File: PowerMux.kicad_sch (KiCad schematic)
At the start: 44 parts, among them J1 USB_C_Receptacle_USB2.0, J3 Barrel_Jack_Switch, J5 USB_B_Mini, J6 Conn_01x04_Socket, Q3 DMP3036SSD, SW1 SW_SPST, U11 L78L05_SOT89, U2 USBLC6-2SC6, U4 CH32X035G8U6, U8 AO3400A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

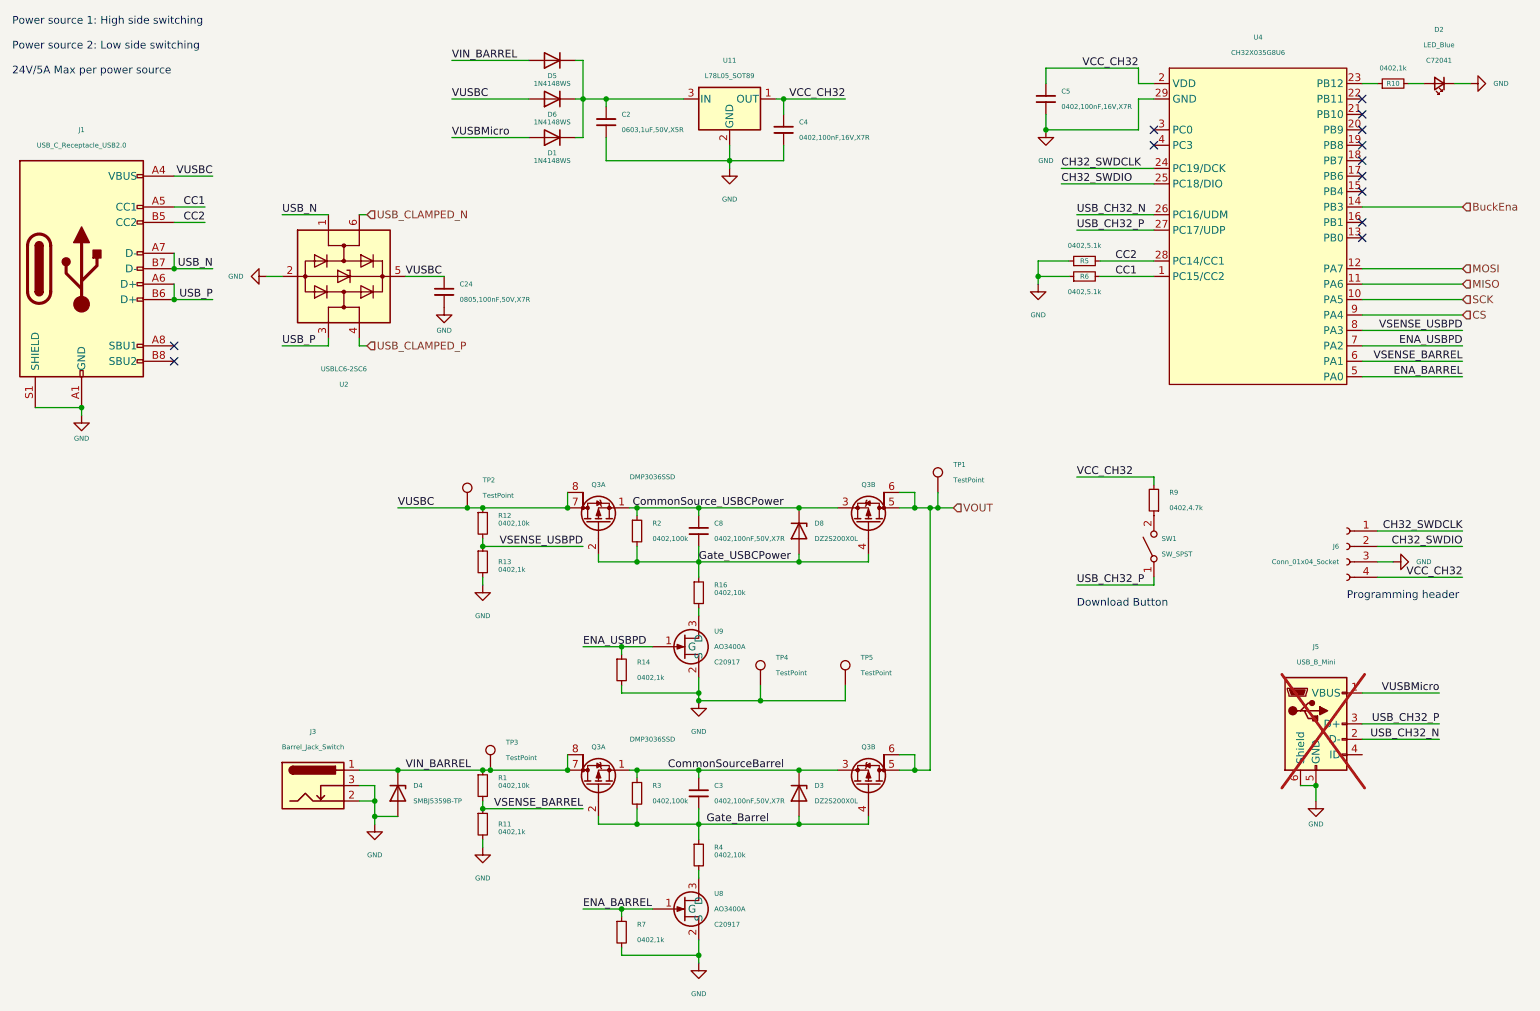
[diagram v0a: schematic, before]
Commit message: updated schematic to look neater
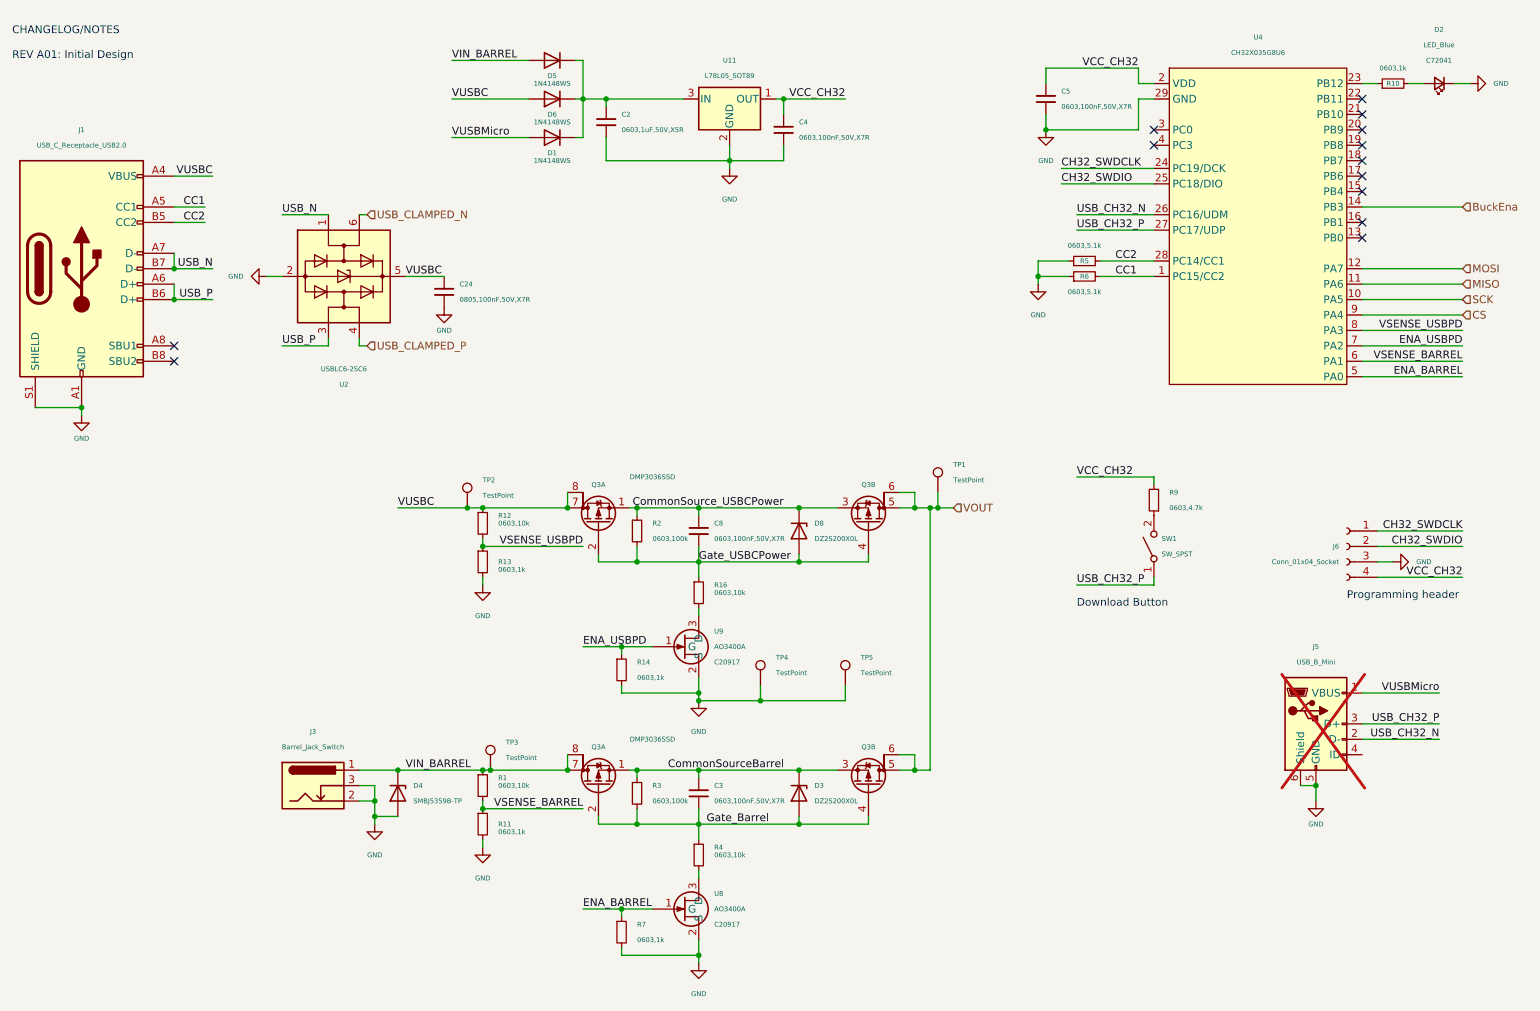
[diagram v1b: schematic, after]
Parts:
- C3, C8: value 0402,100nF,50V,X7R -> 0603,100nF,50V,X7R
- C4, C5: value 0402,100nF,16V,X7R -> 0603,100nF,50V,X7R
- R1, R12, R16, R4: value 0402,10k -> 0603,10k
- R10, R11, R13, R14, R7: value 0402,1k -> 0603,1k
- R2, R3: value 0402,100k -> 0603,100k
- R5, R6: value 0402,5.1k -> 0603,5.1k
- R9: value 0402,4.7k -> 0603,4.7k
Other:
- note added: "CHANGELOG/NOTES REV A01: Initial Design"
- note removed: "Power source 1: High side switching Power source 2: Low side switching 24V/5A Max per power source"
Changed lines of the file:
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@@
   (paper "USLetter")
   (title_block
-    (date "2024-01-28")
+    (date "2024-02-03")
     (rev "A01")
   )
@@
     (stroke (width 0) (type default))
   )
-  (text "Power source 1: High side switching\n\nPower source 2: Low side switching\n\n24V/5A Max per power source"
-    (at 15.24 26.67 0)
-    (effects (font (size 1.27 1.27)) (justify left bottom))
-  )
   (text "Programming header" (at 234.95 113.03 0)
     (effects (font (size 1.27 1.27)) (justify left bottom))
@@
     (effects (font (size 1.27 1.27)) (justify left bottom))
   )
+  (text "CHANGELOG/NOTES\n\nREV A01: Initial Design\n" (at 15.24 24.13 0)
+    (effects (font (size 1.27 1.27)) (justify left bottom))
+  )
   (label "VSENSE_BARREL" (at 109.22 147.32 180) (fields_autoplaced)
     (effects (font (size 1.27 1.27)) (justify right bottom))
@@
       (effects (font (size 0.8 0.8)) (justify left))
     )
-    (property "Value" "0402,100nF,16V,X7R " (at 144.78 36.83 0)
+    (property "Value" "0603,100nF,50V,X7R " (at 144.78 36.83 0)
       (effects (font (size 0.8 0.8)) (justify left))
     )
@@
       (effects (font (size 0.8 0.8)) (justify left))
     )
-    (property "Value" "0402,10k" (at 95.25 100.33 0)
+    (property "Value" "0603,10k" (at 95.25 100.33 0)
       (effects (font (size 0.8 0.8)) (justify left))
     )
@@
       (effects (font (size 0.8 0.8)))
     )
-    (property "Value" "0402,5.1k" (at 191.77 54.61 90)
+    (property "Value" "0603,5.1k" (at 191.77 54.61 90)
       (effects (font (size 0.8 0.8)))
     )
@@
       (effects (font (size 0.8 0.8)) (justify left))
     )
-    (property "Value" "0402,100nF,50V,X7R " (at 130.81 146.05 0)
+    (property "Value" "0603,100nF,50V,X7R " (at 130.81 146.05 0)
       (effects (font (size 0.8 0.8)) (justify left))
     )
@@
       (effects (font (size 0.8 0.8)) (justify left))
     )
-    (property "Value" "0402,10k" (at 130.81 154.94 0)
+    (property "Value" "0603,10k" (at 130.81 154.94 0)
       (effects (font (size 0.8 0.8)) (justify left))
     )
@@
       (effects (font (size 0.8 0.8)) (justify left))
     )
-    (property "Value" "0402,100k" (at 120.65 102.87 0)
+    (property "Value" "0603,100k" (at 120.65 102.87 0)
       (effects (font (size 0.8 0.8)) (justify left))
     )
@@
       (effects (font (size 0.8 0.8)) (justify left))
     )
-    (property "Value" "0402,1k" (at 95.25 151.13 0)
+    (property "Value" "0603,1k" (at 95.25 151.13 0)
       (effects (font (size 0.8 0.8)) (justify left))
     )
@@
       (effects (font (size 0.8 0.8)) (justify left))
     )
-    (property "Value" "0402,1k" (at 118.11 168.91 0)
+    (property "Value" "0603,1k" (at 118.11 168.91 0)
       (effects (font (size 0.8 0.8)) (justify left))
     )
@@
       (effects (font (size 0.8 0.8)) (justify right))
     )
-    (property "Value" "0402,4.7k" (at 205.74 97.79 0)
+    (property "Value" "0603,4.7k" (at 205.74 97.79 0)
       (effects (font (size 0.8 0.8)) (justify right))
     )
@@
       (effects (font (size 0.8 0.8)) (justify left))
     )
-    (property "Value" "0402,1k" (at 95.25 107.95 0)
+    (property "Value" "0603,1k" (at 95.25 107.95 0)
       (effects (font (size 0.8 0.8)) (justify left))
     )
@@
       (effects (font (size 0.8 0.8)) (justify left))
     )
-    (property "Value" "0402,10k" (at 130.81 111.76 0)
+    (property "Value" "0603,10k" (at 130.81 111.76 0)
       (effects (font (size 0.8 0.8)) (justify left))
     )
@@
       (effects (font (size 0.8 0.8)) (justify left))
     )
-    (property "Value" "0402,100nF,50V,X7R " (at 130.81 102.87 0)
+    (property "Value" "0603,100nF,50V,X7R " (at 130.81 102.87 0)
       (effects (font (size 0.8 0.8)) (justify left))
     )
@@
       (effects (font (size 0.8 0.8)))
     )
-    (property "Value" "0402,1k" (at 242.57 25.4 90)
+    (property "Value" "0603,1k" (at 242.57 25.4 90)
       (effects (font (size 0.8 0.8)))
     )
@@
       (effects (font (size 0.8 0.8)) (justify left))
     )
-    (property "Value" "0402,1k" (at 118.11 125.73 0)
+    (property "Value" "0603,1k" (at 118.11 125.73 0)
       (effects (font (size 0.8 0.8)) (justify left))
     )
@@
       (effects (font (size 0.8 0.8)) (justify left))
     )
-    (property "Value" "0402,10k" (at 95.25 143.51 0)
+    (property "Value" "0603,10k" (at 95.25 143.51 0)
       (effects (font (size 0.8 0.8)) (justify left))
     )
@@
       (effects (font (size 0.8 0.8)) (justify left))
     )
-    (property "Value" "0402,100k" (at 120.65 146.05 0)
+    (property "Value" "0603,100k" (at 120.65 146.05 0)
       (effects (font (size 0.8 0.8)) (justify left))
     )
@@
       (effects (font (size 0.8 0.8)) (justify left))
     )
-    (property "Value" "0402,100nF,16V,X7R " (at 187.96 31.75 0)
+    (property "Value" "0603,100nF,50V,X7R " (at 187.96 31.75 0)
       (effects (font (size 0.8 0.8)) (justify left))
     )
@@
       (effects (font (size 0.8 0.8)))
     )
-    (property "Value" "0402,5.1k" (at 191.77 62.23 90)
-      (effects (font (size 0.8 0.8)))
-    )
+    (property "Value" "0603,5.1k" (at 191.77 62.23 90)
+      (effects (font (size 0.8 0.8)))
+    )
